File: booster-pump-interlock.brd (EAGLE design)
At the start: 63.5 x 50.8 mm, 17 parts, among them IC1 OPA743, IC2 OPA743, IC3 4044D, IC4 OPA743, IC5 OPA743

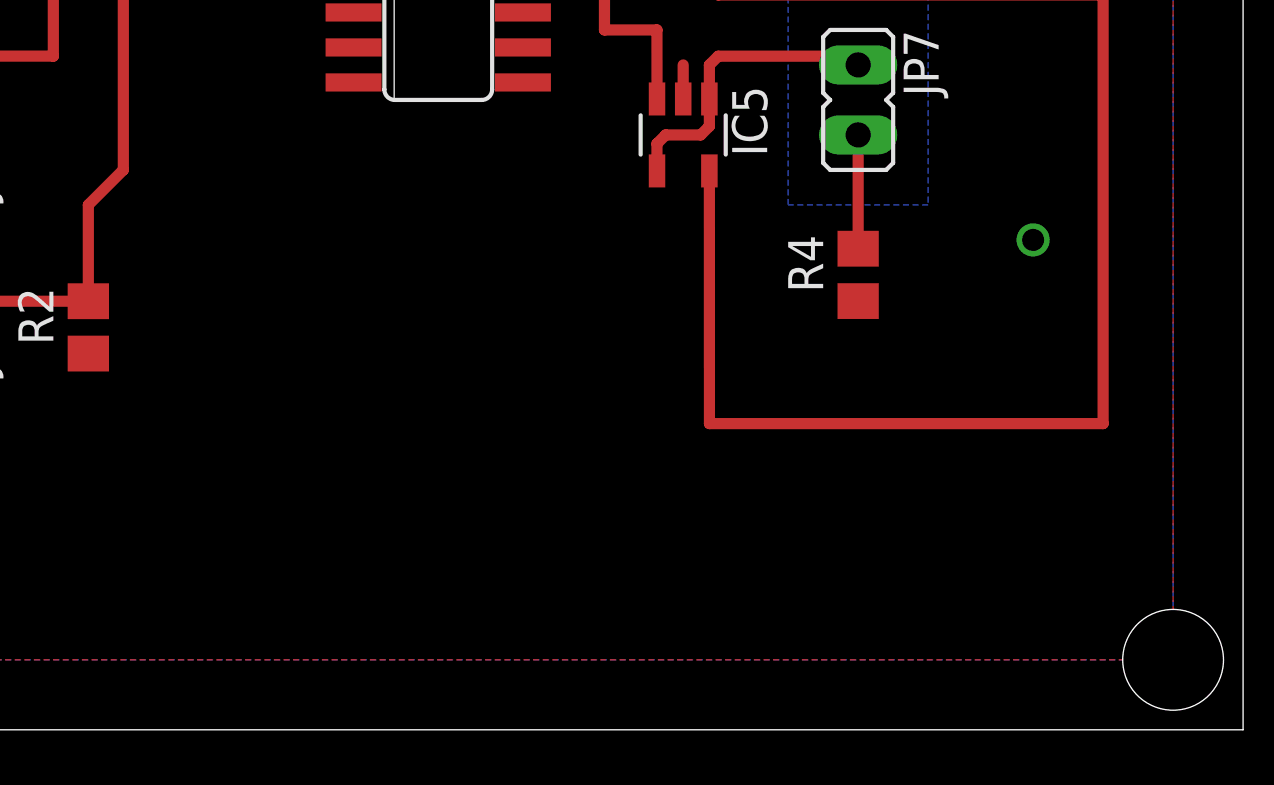
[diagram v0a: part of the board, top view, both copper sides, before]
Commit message: added QR code & tag.
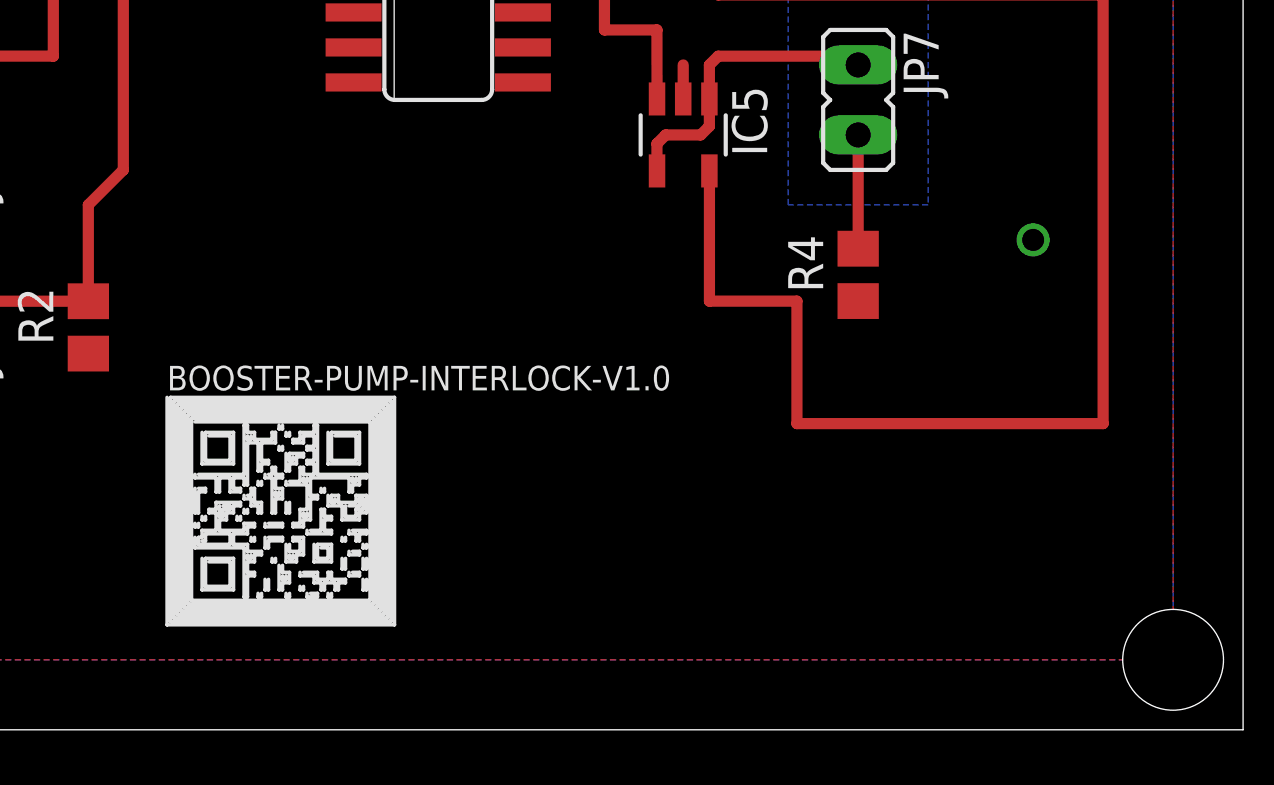
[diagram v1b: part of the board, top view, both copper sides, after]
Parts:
- added BOOSTER-PUMP-INTERLOCK-V1.0: QR-HTTP://GIT.IO/V5BSG-WIRE, QR-git.io-v5bSG:QR-HTTP://GIT.IO/V5BSG-WIRE
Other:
- board text removed: "Documentation: https://git.io/v5bSG Tag: v1.0"
- board text removed: "booster-pump-interlock"
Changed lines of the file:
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@@
 <hole x="60.96" y="48.26" drill="3.6576"/>
 <hole x="60.96" y="2.54" drill="3.6576"/>
-<text x="22.86" y="3.81" size="1.778" layer="51">Documentation:
-https://git.io/v5bSG
-Tag: v1.0 </text>
-<text x="34.29" y="45.72" size="1.778" layer="51">booster-pump-interlock</text>
 </plain>
 <attributes>
@@
 <element name="R4" library="rcl" package="R0805" value="150" x="49.53" y="16.51" rot="R90"/>
 <element name="R5" library="rcl" package="R0805" value="10k" x="49.53" y="30.48" rot="R90"/>
+<element name="BOOSTER-PUMP-INTERLOCK-V1.0" library="QR-git.io-v5bSG" package="QR-HTTP://GIT.IO/V5BSG-WIRE" value="QR-HTTP://GIT.IO/V5BSG-WIRE" x="28.575" y="7.9375">
+<attribute name="QR_DEST" value="http://git.io/v5bSG" x="28.575" y="7.9375" size="1.778" layer="27" display="off"/>
+<attribute name="QR_DEST_SHORT" value="git.io/v5bSG" x="28.575" y="7.9375" size="1.778" layer="27" display="off"/>
+</element>
 </elements>
 <signals>
@@
 <wire x1="39.37" y1="36.83" x2="39.37" y2="44.45" width="0.4064" layer="1"/>
 <wire x1="39.37" y1="44.45" x2="15.24" y2="44.45" width="0.4064" layer="1"/>
-<wire x1="44.13" y1="20.284" x2="44.1325" y2="11.1125" width="0.4064" layer="1"/>
-<wire x1="44.1325" y1="11.1125" x2="58.42" y2="11.1125" width="0.4064" layer="1"/>
 <wire x1="58.42" y1="11.1125" x2="58.42" y2="26.67" width="0.4064" layer="1"/>
 <wire x1="58.42" y1="26.67" x2="58.42" y2="36.83" width="0.4064" layer="1"/>
@@
 <wire x1="44.1325" y1="26.9875" x2="44.45" y2="26.67" width="0.4064" layer="1"/>
 <wire x1="44.45" y1="26.67" x2="58.42" y2="26.67" width="0.4064" layer="1"/>
+<wire x1="44.13" y1="20.284" x2="44.1325" y2="20.284" width="0.4064" layer="1"/>
+<wire x1="44.1325" y1="20.284" x2="44.1325" y2="15.5575" width="0.4064" layer="1"/>
+<wire x1="44.1325" y1="15.5575" x2="47.3075" y2="15.5575" width="0.4064" layer="1"/>
+<wire x1="47.3075" y1="15.5575" x2="47.3075" y2="11.1125" width="0.4064" layer="1"/>
+<wire x1="47.3075" y1="11.1125" x2="58.42" y2="11.1125" width="0.4064" layer="1"/>
 </signal>
 <signal name="GND">
@@
 </board>
 </drawing>
-<compatibility>
-<note version="6.3" minversion="6.2.2" severity="warning">
-Since Version 6.2.2 text objects can contain more than one line,
-which will not be processed correctly with this version.
-</note>
-</compatibility>
 </eagle>

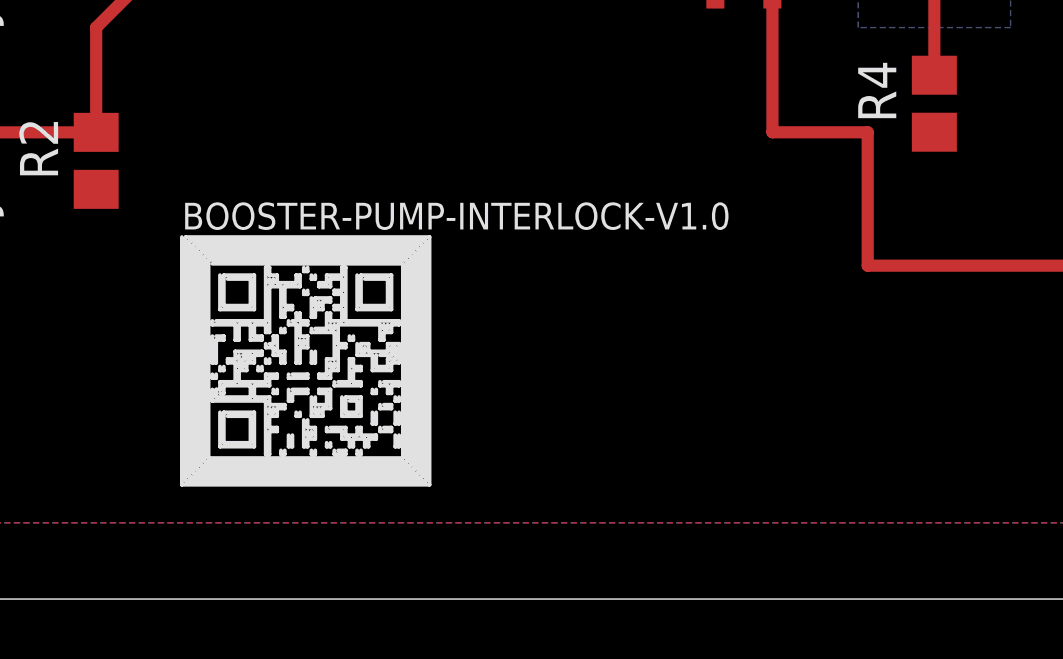
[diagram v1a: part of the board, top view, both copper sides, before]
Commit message: added QR code & tag.
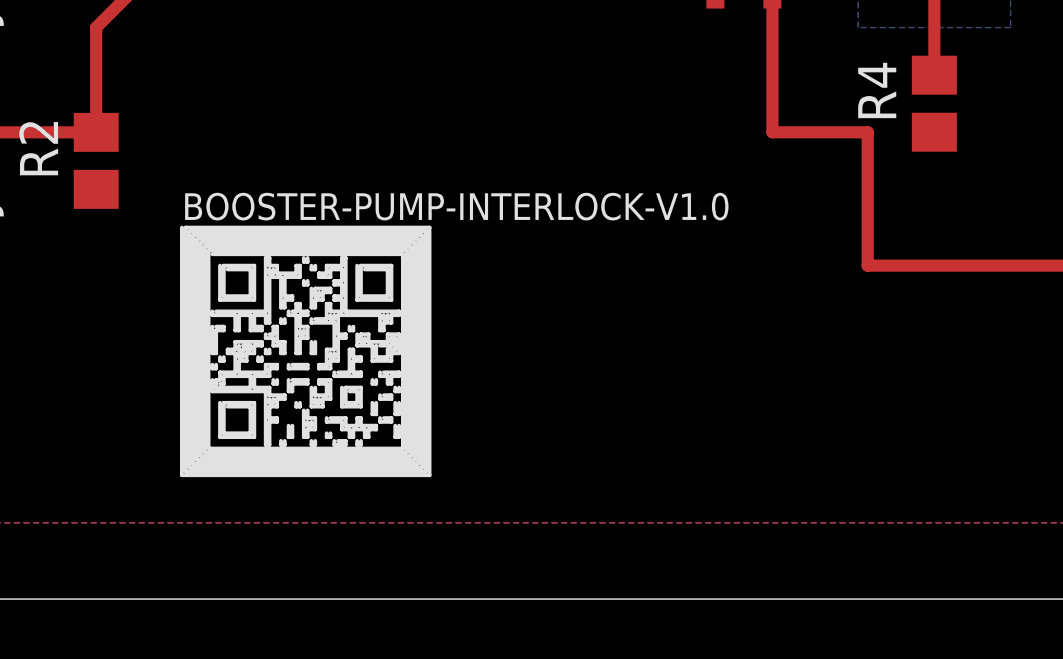
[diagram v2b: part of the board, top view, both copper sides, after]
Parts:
- moved BOOSTER-PUMP-INTERLOCK-V1.0 0.32 mm to (28.6, 8.26)
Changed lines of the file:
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@@
 <element name="R4" library="rcl" package="R0805" value="150" x="49.53" y="16.51" rot="R90"/>
 <element name="R5" library="rcl" package="R0805" value="10k" x="49.53" y="30.48" rot="R90"/>
-<element name="BOOSTER-PUMP-INTERLOCK-V1.0" library="QR-git.io-v5bSG" package="QR-HTTP://GIT.IO/V5BSG-WIRE" value="QR-HTTP://GIT.IO/V5BSG-WIRE" x="28.575" y="7.9375">
-<attribute name="QR_DEST" value="http://git.io/v5bSG" x="28.575" y="7.9375" size="1.778" layer="27" display="off"/>
-<attribute name="QR_DEST_SHORT" value="git.io/v5bSG" x="28.575" y="7.9375" size="1.778" layer="27" display="off"/>
+<element name="BOOSTER-PUMP-INTERLOCK-V1.0" library="QR-git.io-v5bSG" package="QR-HTTP://GIT.IO/V5BSG-WIRE" value="QR-HTTP://GIT.IO/V5BSG-WIRE" x="28.575" y="8.255">
+<attribute name="QR_DEST" value="http://git.io/v5bSG" x="28.575" y="8.255" size="1.778" layer="27" display="off"/>
+<attribute name="QR_DEST_SHORT" value="git.io/v5bSG" x="28.575" y="8.255" size="1.778" layer="27" display="off"/>
 </element>
 </elements>

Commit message: added QR code & tag.
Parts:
- renumbered BOOSTER-PUMP-INTERLOCK-V1.0 to BOOSTER-PUMP-INTERLOCK-V1.1
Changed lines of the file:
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@@
 <element name="R4" library="rcl" package="R0805" value="150" x="49.53" y="16.51" rot="R90"/>
 <element name="R5" library="rcl" package="R0805" value="10k" x="49.53" y="30.48" rot="R90"/>
-<element name="BOOSTER-PUMP-INTERLOCK-V1.0" library="QR-git.io-v5bSG" package="QR-HTTP://GIT.IO/V5BSG-WIRE" value="QR-HTTP://GIT.IO/V5BSG-WIRE" x="28.575" y="8.255">
+<element name="BOOSTER-PUMP-INTERLOCK-V1.1" library="QR-git.io-v5bSG" package="QR-HTTP://GIT.IO/V5BSG-WIRE" value="QR-HTTP://GIT.IO/V5BSG-WIRE" x="28.575" y="8.255">
 <attribute name="QR_DEST" value="http://git.io/v5bSG" x="28.575" y="8.255" size="1.778" layer="27" display="off"/>
 <attribute name="QR_DEST_SHORT" value="git.io/v5bSG" x="28.575" y="8.255" size="1.778" layer="27" display="off"/>

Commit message: Added pulldown resistor to fix tripping issue due to charge buildup on pulldown diode
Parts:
- added R6: 10k, rcl:M1206
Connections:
- net GND: now also R6.1
- net S0: now also R6.2
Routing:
- net S0: track 11.2 -> 11.9 mm
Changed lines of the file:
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@@
 <?xml version="1.0" encoding="utf-8"?>
 <!DOCTYPE eagle SYSTEM "eagle.dtd">
-<eagle version="7.7.0">
+<eagle version="9.0.1">
 <drawing>
 <settings>
 <setting alwaysvectorfont="no"/>
+<setting keepoldvectorfont="yes"/>
 <setting verticaltext="up"/>
 </settings>
@@
 <param name="dpMaxLengthDifference" value="10mm"/>
 <param name="dpGapFactor" value="2.5"/>
-<param name="checkGrid" value="0"/>
 <param name="checkAngle" value="0"/>
 <param name="checkFont" value="1"/>
 <param name="checkRestrict" value="1"/>
+<param name="checkStop" value="0"/>
+<param name="checkValues" value="0"/>
 <param name="useDiameter" value="13"/>
 <param name="maxErrors" value="50"/>
@@
 <attribute name="QR_DEST_SHORT" value="git.io/v5bSG" x="28.575" y="8.255" size="1.778" layer="27" display="off"/>
 </element>
+<element name="R6" library="rcl" package="M1206" value="10k" x="28.575" y="28.575" rot="R90"/>
 </elements>
 <signals>
@@
 <contactref element="JP5" pad="2"/>
 <contactref element="JP6" pad="2"/>
+<contactref element="R6" pad="1"/>
 </signal>
 <signal name="N$2">
@@
 <contactref element="JP5" pad="1"/>
 <wire x1="25.7175" y1="32.0675" x2="27.305" y2="32.0675" width="0.4064" layer="1"/>
-<wire x1="27.305" y1="32.0675" x2="29.5275" y2="29.845" width="0.4064" layer="1"/>
+<wire x1="27.305" y1="32.0675" x2="29.21" y2="30.1625" width="0.4064" layer="1"/>
+<wire x1="29.21" y1="30.1625" x2="29.5275" y2="29.845" width="0.4064" layer="1"/>
 <wire x1="29.5275" y1="29.845" x2="31.2166" y2="29.845" width="0.4064" layer="1"/>
 <wire x1="25.7175" y1="32.0675" x2="25.7175" y2="36.83" width="0.4064" layer="1"/>
+<contactref element="R6" pad="2"/>
+<wire x1="28.575" y1="29.975" x2="28.7625" y2="30.1625" width="0.4064" layer="1"/>
+<wire x1="28.7625" y1="30.1625" x2="29.21" y2="30.1625" width="0.4064" layer="1"/>
 </signal>
 <signal name="Q0">
